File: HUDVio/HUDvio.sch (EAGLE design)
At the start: 16 parts, among them U1 ST_STM32F446RET7, U3 TVP5150AM1PBSR, X1 ABRACON_ABM8-27.000MHZ

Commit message: Lots of shit. Added splitter
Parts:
- added C10: 30PF_0805, Skyhawkson-Capacitors:30PF_0805
- added C11, C12, C13: 1UF_0805, Skyhawkson-Capacitors:1UF_0805
- added C14, C15, C16, C17, C18, C19, C20, C4, C7, C8, C9: 100NF_0805, Skyhawkson-Capacitors:100NF_0805
- added C5, C6: 10UF_0805, Skyhawkson-Capacitors:10UF_0805
- added R10, R11, R12, R16, R18, R9: 1K_0603, Skyhawkson-Resistors:1K_0603
- added R13: 0R_0603, Skyhawkson-Resistors:0R_0603
- added R14, R15: 37R4_0603, Skyhawkson-Resistors:37R4_0603
- added R17, R7, R8: 75R_0603, Skyhawkson-Resistors:75R_0603
- added U4: NEXPERIA_NVT2006, Skyhawkson-ICs:NEXPERIA_NVT2006
- added U5: MAXIM_MAX4389, Skyhawkson-RF:MAXIM_MAX4389
- added X2: ABRACON_ABM8-14.31818MHZ, Skyhawkson-Miscellaneous:ABRACON_ABM8-14.31818MHZ
- C1: value 1UF_0805 -> 30PF_0805; device Skyhawkson-Capacitors:1UF_0805 -> Skyhawkson-Capacitors:30PF_0805
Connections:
- removed net VIDEO-OUT: U$3.3
- new net $NET11: C7.2, R13.1, R7.1
- new net +1V8: C16.2, C17.2, C18.2, C19.2, U3.AVDD@4,32, U3.DVDD@20
- new net +3V3: C14.2, R11.1, U3.IO_DVDD@10, U4.VREFA@2
- new net 5150-IN: C20.2, U3.AIP1A@1
- new net ACTIVE-VID: U3.AVID@26
- new net CS-LV: U4.A1
- new net FID/GLCO: U3.FID/GLCO@23
- new net LOS-LV: U4.A5
- new net LOSS-OF-SYNC: R9.1, U2.LOS@12, U4.B5
- new net MAX7456-OUT: R8.2
- new net MISO-LV: U4.A4
- new net MOSI-LV: U4.A2
- new net N$10: C5.2, C6.2, R8.1
- new net N$11: C20.1, R14.2, R15.2
- new net N$12: C15.2, U3.AIP1B@2
- new net N$13: R16.1, U4.EN@16
- new net N$14: U5.IN+@3
- new net N$15: R18.1, U5.IN-@4
- new net N$6: R10.2, U3.!RESETB!@8
- new net N$7: R12.2, U3.PDN@28
- new net N$8: C11.1, C13.1, U3.REFM@30
- new net N$9: C11.2, C12.2, U3.REFP@29
- new net SAG: C6.1, U2.SAG@25
- new net SCLK-LV: U4.A3
- new net SPLITTER-OUT: R14.1, R17.1, U5.OUT@1
- new net SYSCLK: U3.SCLK@9
- new net VBLANK: U3.INTREQ/GPCL/VBLK@27
- new net VIDIN: C7.1, U2.VIDIN@22
- new net VIDOUT: C5.1, U2.VIDOUT@26
- new net VTX-OUT: R17.2, U$3.3
- new net XTAL1: C1.1, U3.XTAL1@5, X2.1
- new net XTAL2: C10.1, U3.XTAL2@6, X2.3
- new net YOUT0: U3.YOUT0@18
- new net YOUT1: U3.YOUT1@17
- new net YOUT2: U3.YOUT2@16
- new net YOUT3: U3.YOUT3@15
- new net YOUT4: U3.YOUT4@14
- new net YOUT5: U3.YOUT5@13
- new net YOUT6: U3.YOUT6@12
- new net YOUT7: R11.2, U3.YOUT7/I2CSEL@11
- net +5V: now also C4.2, C8.2, C9.2, R10.1, R12.1, R16.2, R9.2, U2.AVDD@21, U2.PVDD@24, U4.VREFB@15, U5.VCC@6; no longer C1.2
- net GND: now also C1.2, C10.2, C12.1, C13.2, C14.1, C15.1, C16.1, C17.1, C18.1, C19.1, C4.1, C8.1, C9.1, R15.1, R18.2, R7.2, U2.AGND@20, U2.PGND@23, U3.AGND@3,7,31, U3.DGND@19, U4.GND@1, U5.VEE@2, X2.2, X2.4; no longer C1.1
- net MAX7456-CS: now also U4.B1
- net MISO: now also U4.B4
- net MOSI: now also U4.B2
- net SCLK: now also U4.B3
- net VIDEO-IN: now also R13.2
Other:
- note added: "(2*18pF) - 6pF = 30pF"
- note added: "(May not be needed due to splitter, if so pop. with 0R)"
- note added: "0R for potential divider"
- note added: "10uF COUT and CSAG save space at the cost of timing distortion .6%"
- note added: "Bidirectional Level Shifter for Comms. w/MAX7456"
- note added: "DVDD and AVDD decoupling caps"
- note added: "Divider to attenuate the 2x gain from the MAX7456"
- note added: "External Solder Points"
- note added: "MAX7456 On-Screen Display"
- note added: "RGB LED - PWM Dimmed"
- note added: "SYSCLK: 2x PIXCLK Freq."
- note added: "Splitter to VTX"
- note added: "TVP5150 Video Decoding"
- note added: "VBLANK used as active-high interrupt"
- note added: "YOUT7 pulled high sets I2C addr. to BAh upon chip startup"
- moved on the sheet: C1, C2, C3, D1, R1, R2, R3, R4, R5, R6, U2, U3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

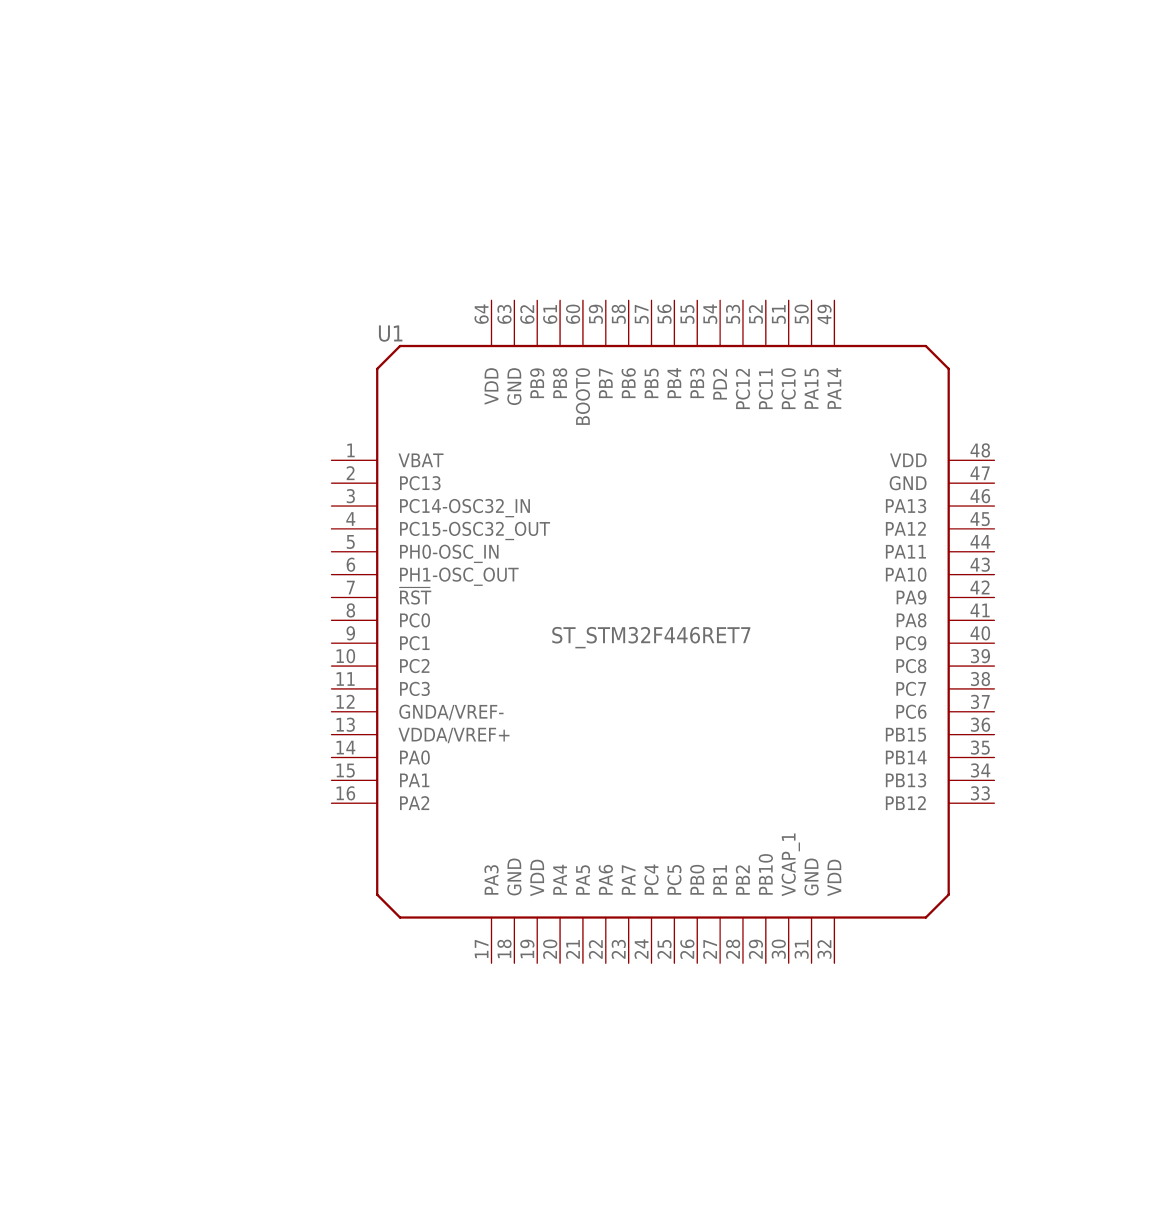
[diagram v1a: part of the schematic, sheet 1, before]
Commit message: Ran DCMI pins
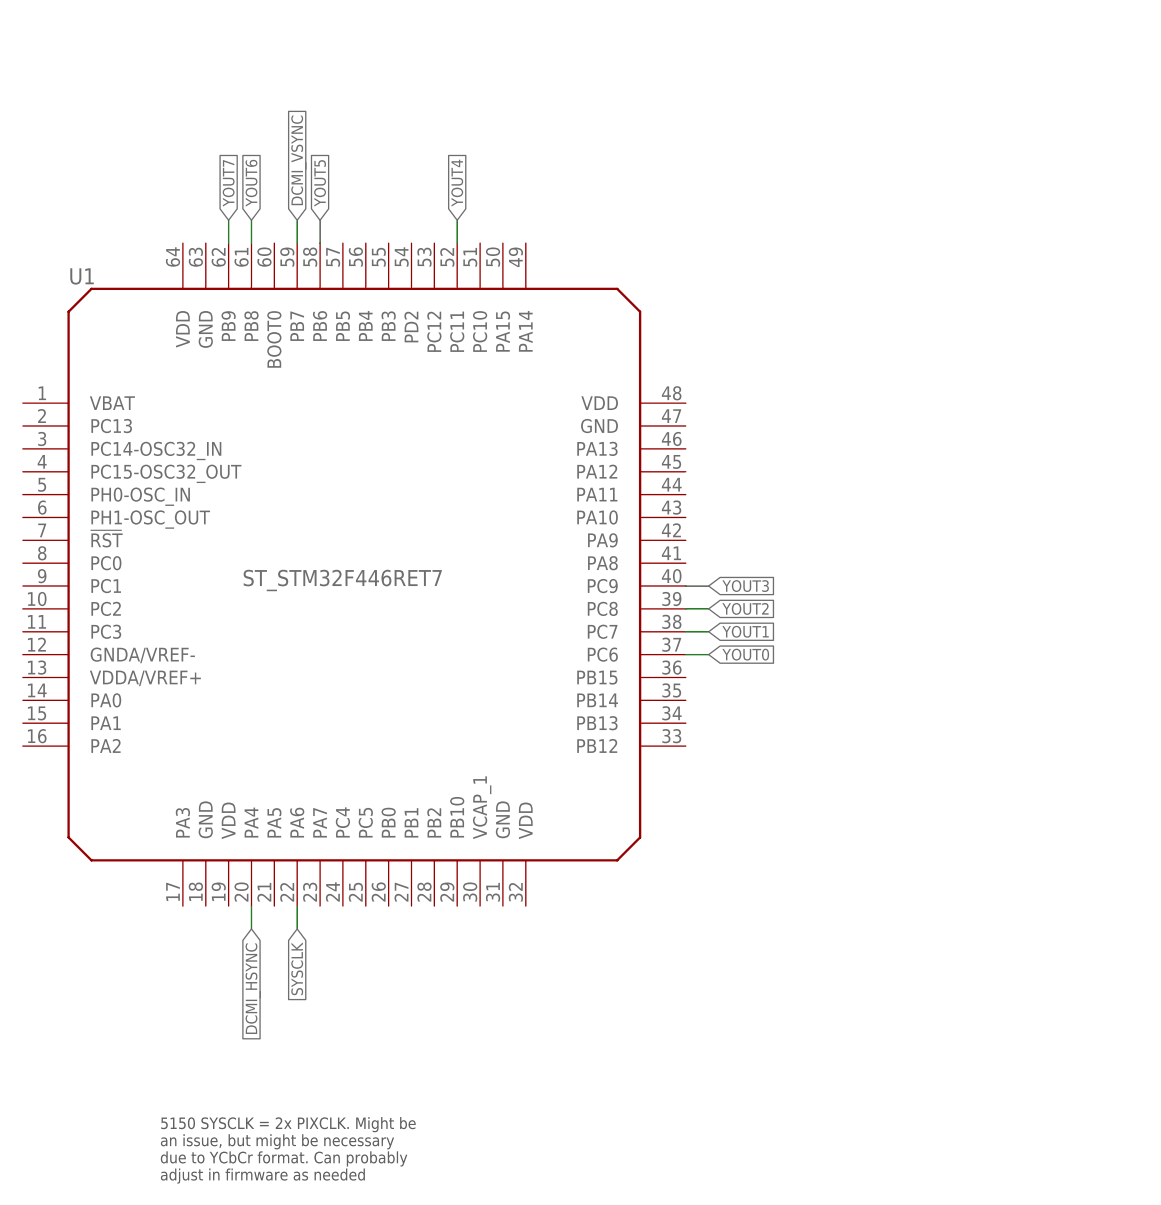
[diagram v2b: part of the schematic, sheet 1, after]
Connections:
- new net DCMI_HSYNC: U1.PA4@20, U3.HSYNC@25
- new net DCMI_VSYNC: U1.PB7@59, U3.VSYNC/PALI@24
- net SYSCLK: now also U1.PA6@22
- net YOUT0: now also U1.PC6@37
- net YOUT1: now also U1.PC7@38
- net YOUT2: now also U1.PC8@39
- net YOUT3: now also U1.PC9@40
- net YOUT4: now also U1.PC11@52
- net YOUT5: now also U1.PB6@58
- net YOUT6: now also U1.PB8@61
- net YOUT7: now also U1.PB9@62
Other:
- note added: "5150 SYSCLK = 2x PIXCLK. Might be an issue, but might be necessary due to YCbCr format. Can probably adjust in firmware as needed"
- moved on the sheet: U1
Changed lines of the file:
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@@
 <wire x1="172.72" y1="81.28" x2="172.72" y2="121.92" width="0.1524" layer="97" style="shortdash"/>
 <text x="172.72" y="122.174" size="1.27" layer="97">Bidirectional Level Shifter for Comms. w/MAX7456</text>
+<text x="53.34" y="40.64" size="1.27" layer="97">5150 SYSCLK = 2x PIXCLK. Might be
+an issue, but might be necessary
+due to YCbCr format. Can probably
+adjust in firmware as needed</text>
 </plain>
 <instances>
@@
 <attribute name="SHEET" x="230.505" y="5.08" size="2.54" layer="94"/>
 </instance>
-<instance part="U1" gate="G$1" x="72.39" y="120.65" smashed="yes">
-<attribute name="VALUE" x="107.95" y="100.33" size="1.778" layer="96" align="bottom-center"/>
-<attribute name="NAME" x="77.47" y="133.858" size="1.778" layer="95"/>
+<instance part="U1" gate="G$1" x="38.1" y="127" smashed="yes">
+<attribute name="VALUE" x="73.66" y="106.68" size="1.778" layer="96" align="bottom-center"/>
+<attribute name="NAME" x="43.18" y="140.208" size="1.778" layer="95"/>
 </instance>
 <instance part="D1" gate="G$1" x="203.2" y="152.4" smashed="yes">
@@
 <wire x1="185.42" y1="88.9" x2="177.8" y2="88.9" width="0.1524" layer="91"/>
 <label x="177.8" y="88.9" size="1.27" layer="95"/>
+</segment>
+</net>
+<net name="YOUT7" class="0">
+<segment>
+<label x="60.96" y="147.32" size="1.27" layer="95" rot="MR90" xref="yes"/>
+<pinref part="U1" gate="G$1" pin="PB9@62"/>
+<wire x1="60.96" y1="147.32" x2="60.96" y2="144.78" width="0.1524" layer="91"/>
+</segment>
+</net>
+<net name="YOUT0" class="0">
+<segment>
+<wire x1="111.76" y1="99.06" x2="114.3" y2="99.06" width="0.1524" layer="91"/>
+<label x="114.3" y="99.06" size="1.27" layer="95" xref="yes"/>
+<pinref part="U1" gate="G$1" pin="PC6@37"/>
+</segment>
+</net>
+<net name="YOUT1" class="0">
+<segment>
+<wire x1="111.76" y1="101.6" x2="114.3" y2="101.6" width="0.1524" layer="91"/>
+<label x="114.3" y="101.6" size="1.27" layer="95" xref="yes"/>
+<pinref part="U1" gate="G$1" pin="PC7@38"/>
+</segment>
+</net>
+<net name="YOUT2" class="0">
+<segment>
+<wire x1="111.76" y1="104.14" x2="114.3" y2="104.14" width="0.1524" layer="91"/>
+<label x="114.3" y="104.14" size="1.27" layer="95" rot="MR180" xref="yes"/>
+<pinref part="U1" gate="G$1" pin="PC8@39"/>
+</segment>
+</net>
+<net name="YOUT3" class="0">
+<segment>
+<wire x1="111.76" y1="106.68" x2="114.3" y2="106.68" width="0.1524" layer="91"/>
+<label x="114.3" y="106.68" size="1.27" layer="95" rot="MR180" xref="yes"/>
+<pinref part="U1" gate="G$1" pin="PC9@40"/>
+</segment>
+</net>
+<net name="YOUT4" class="0">
+<segment>
+<wire x1="86.36" y1="144.78" x2="86.36" y2="147.32" width="0.1524" layer="91"/>
+<label x="86.36" y="147.32" size="1.27" layer="95" rot="MR90" xref="yes"/>
+<pinref part="U1" gate="G$1" pin="PC11@52"/>
+</segment>
+</net>
+<net name="YOUT5" class="0">
+<segment>
+<wire x1="71.12" y1="144.78" x2="71.12" y2="147.32" width="0.1524" layer="91"/>
+<label x="71.12" y="147.32" size="1.27" layer="95" rot="MR90" xref="yes"/>
+<pinref part="U1" gate="G$1" pin="PB6@58"/>
+</segment>
+</net>
+<net name="YOUT6" class="0">
+<segment>
+<label x="63.5" y="147.32" size="1.27" layer="95" rot="MR90" xref="yes"/>
+<pinref part="U1" gate="G$1" pin="PB8@61"/>
+<wire x1="63.5" y1="147.32" x2="63.5" y2="144.78" width="0.1524" layer="91"/>
+</segment>
+</net>
+<net name="DCMI_HSYNC" class="0">
+<segment>
+<wire x1="63.5" y1="71.12" x2="63.5" y2="68.58" width="0.1524" layer="91"/>
+<label x="63.5" y="68.58" size="1.27" layer="95" rot="R270" xref="yes"/>
+<pinref part="U1" gate="G$1" pin="PA4@20"/>
+</segment>
+</net>
+<net name="DCMI_VSYNC" class="0">
+<segment>
+<wire x1="68.58" y1="144.78" x2="68.58" y2="147.32" width="0.1524" layer="91"/>
+<label x="68.58" y="147.32" size="1.27" layer="95" rot="R90" xref="yes"/>
+<pinref part="U1" gate="G$1" pin="PB7@59"/>
+</segment>
+</net>
+<net name="SYSCLK" class="0">
+<segment>
+<label x="68.58" y="68.58" size="1.27" layer="95" rot="R270" xref="yes"/>
+<pinref part="U1" gate="G$1" pin="PA6@22"/>
+<wire x1="68.58" y1="71.12" x2="68.58" y2="68.58" width="0.1524" layer="91"/>
 </segment>
 </net>
@@
 </segment>
 </net>
-<net name="VIDIN" class="0">
+<net name="VIDIN" class="1">
 <segment>
 <pinref part="U2" gate="G$1" pin="VIDIN@22"/>
@@
 </segment>
 </net>
-<net name="VIDOUT" class="0">
+<net name="VIDOUT" class="1">
 <segment>
 <wire x1="172.72" y1="144.78" x2="172.72" y2="154.94" width="0.1524" layer="91"/>
@@
 </segment>
 </net>
-<net name="MAX7456-OUT" class="0">
+<net name="MAX7456-OUT" class="1">
 <segment>
 <pinref part="R8" gate="G$1" pin="2"/>
@@
 </segment>
 </net>
-<net name="5150-IN" class="0">
+<net name="5150-IN" class="1">
 <segment>
 <pinref part="U3" gate="G$1" pin="AIP1A@1"/>
@@
 </segment>
 </net>
-<net name="SPLITTER-OUT" class="0">
+<net name="SPLITTER-OUT" class="1">
 <segment>
 <pinref part="U5" gate="G$1" pin="OUT@1"/>
@@
 </segment>
 </net>
-<net name="VTX-OUT" class="0">
+<net name="VTX-OUT" class="1">
 <segment>
 <pinref part="R17" gate="G$1" pin="2"/>
@@
 </segment>
 </net>
+<net name="DCMI_HSYNC" class="0">
+<segment>
+<pinref part="U3" gate="G$1" pin="HSYNC@25"/>
+<wire x1="175.26" y1="58.42" x2="180.34" y2="58.42" width="0.1524" layer="91"/>
+<label x="180.34" y="58.42" size="1.27" layer="95" xref="yes"/>
+</segment>
+</net>
+<net name="DCMI_VSYNC" class="0">
+<segment>
+<pinref part="U3" gate="G$1" pin="VSYNC/PALI@24"/>
+<wire x1="175.26" y1="55.88" x2="180.34" y2="55.88" width="0.1524" layer="91"/>
+<label x="180.34" y="55.88" size="1.27" layer="95" xref="yes"/>
+</segment>
+</net>
